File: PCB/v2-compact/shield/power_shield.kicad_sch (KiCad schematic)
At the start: 0 parts

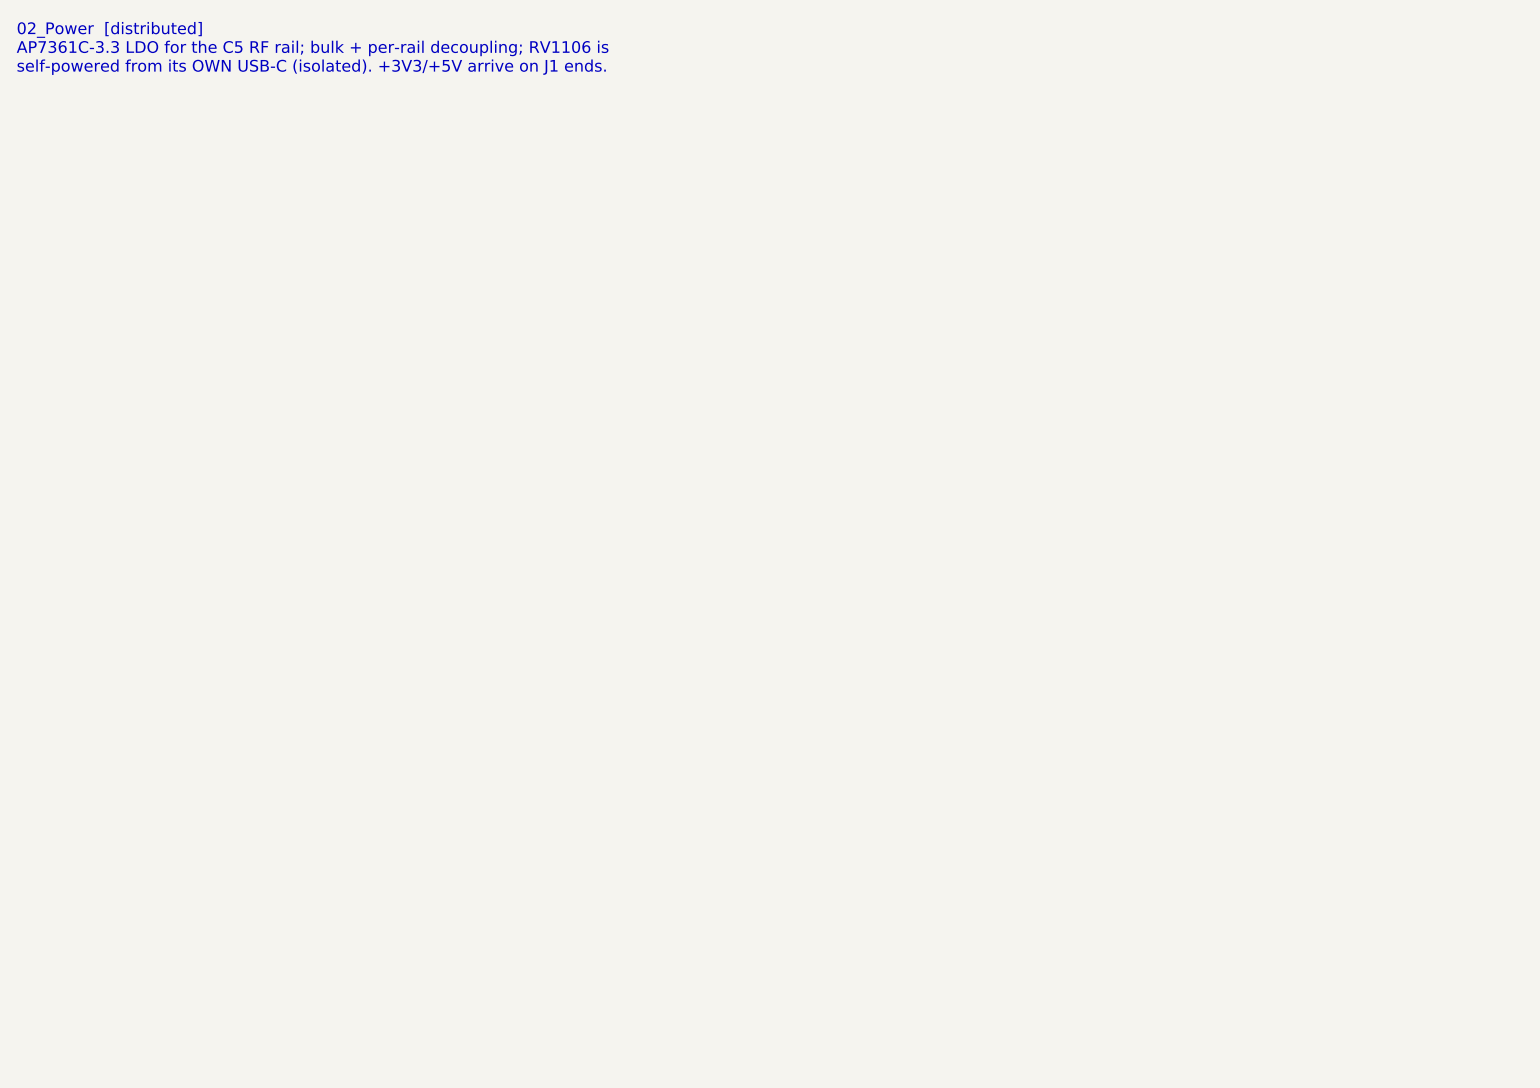
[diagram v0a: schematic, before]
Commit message: Schematics: capture PN532, GPS, IR, and both power sheets
- 07_NFC_PN532: I2C mode (I0/I1 set), 27.12MHz crystal, VMID cap, internal
  DVDD/SVDD regulator outputs correctly decoupled (not tied to 3V3), pull-ups;
  antenna pins flagged for the RF matching pass.
- 10_GPS: NEO-M9N UART to the C5, power + decoupling; bias-tee/antenna flagged.
- 11_IR: TSOP receiver + IR-LED transmitter (NPN driver).
- 02_Power (shield): local AP7361C LDO for the C5 rail + bulk caps + PWR_FLAGs.
- 01_Power_USB (main): USB-C, CC resistors, USBLC6 ESD, AP7361C 3V3 LDO.

All netlist-verified. Remaining ERC items are expected WIP (no-connects on unused
IC pins + power flags), to be cleaned once the MCU sheets tie in the shared nets.
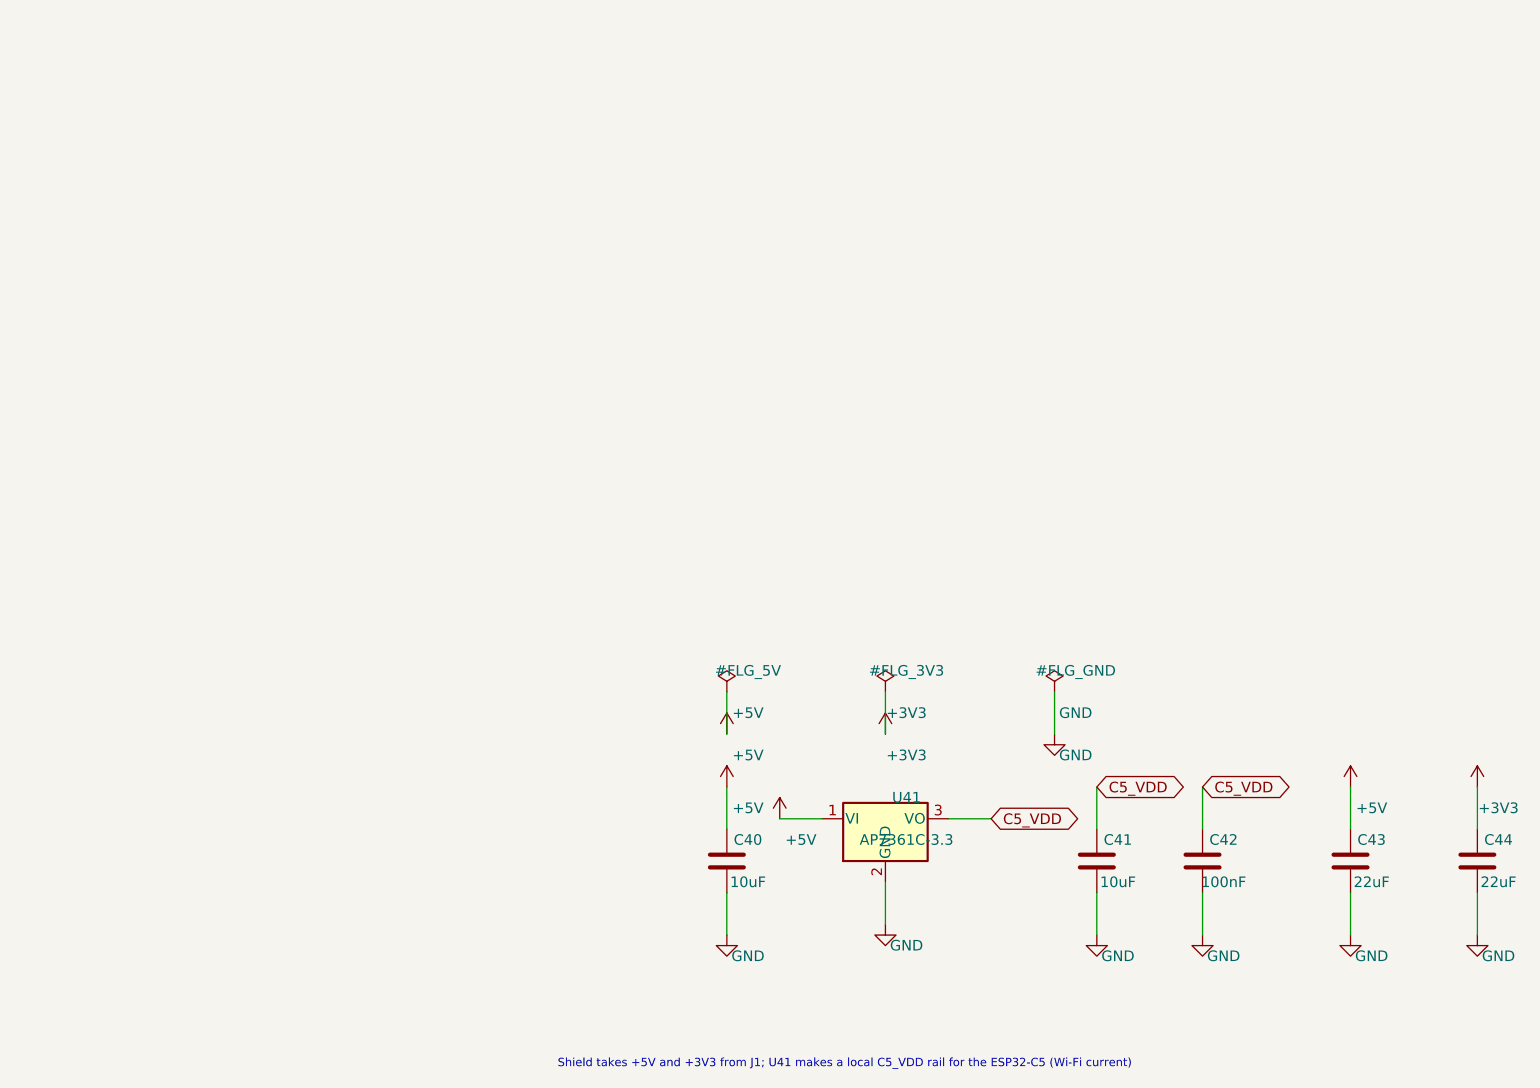
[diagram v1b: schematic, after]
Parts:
- added C40, C41: 10uF, Capacitor_SMD:C_0402_1005Metric, symbol Device:C
- added C42: 100nF, Capacitor_SMD:C_0402_1005Metric, symbol Device:C
- added C43, C44: 22uF, Capacitor_SMD:C_0402_1005Metric, symbol Device:C
- added U41: AP7361C-3.3, Package_TO_SOT_SMD:SOT-23-5, symbol Regulator_Linear:AP7361C-33E
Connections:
- new net +3V3: C44.1
- new net +5V: C40.1, C43.1, U41.1 (VI)
- new net C5_VDD: C41.1, C42.1, U41.3 (VO)
- new net GND: C40.2, C41.2, C42.2, C43.2, C44.2, U41.2 (GND)
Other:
- note added: "Shield takes +5V and +3V3 from J1; U41 makes a local C5_VDD rail for the ESP32-C5 (Wi-Fi current)"
- note removed: "02_Power [distributed] AP7361C-3.3 LDO for the C5 RF rail; bulk + per-rail decoupling; RV1106 is self-powered from its OWN USB-C (isolated). +3V3/+5V arrive on J1 ends."
